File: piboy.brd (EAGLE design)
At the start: 76.2 x 76.2 mm, 69 parts, among them CN4 MicroUSB, T1 MMUN2133LT1G, U1 TPS61090RSAR, U2 MCP73871, U3 TPA2005D1

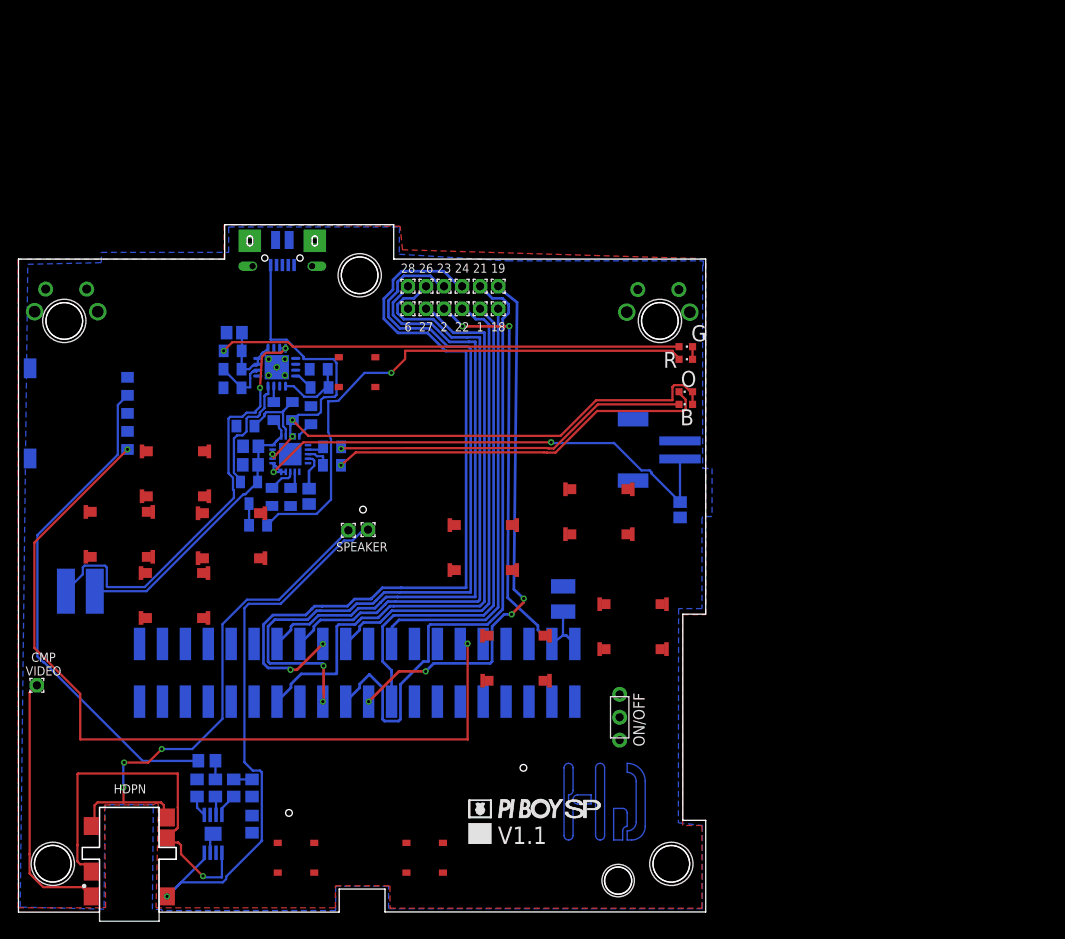
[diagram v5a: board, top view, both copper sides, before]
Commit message: -routed all signals before using the autorouter for voltages and GND
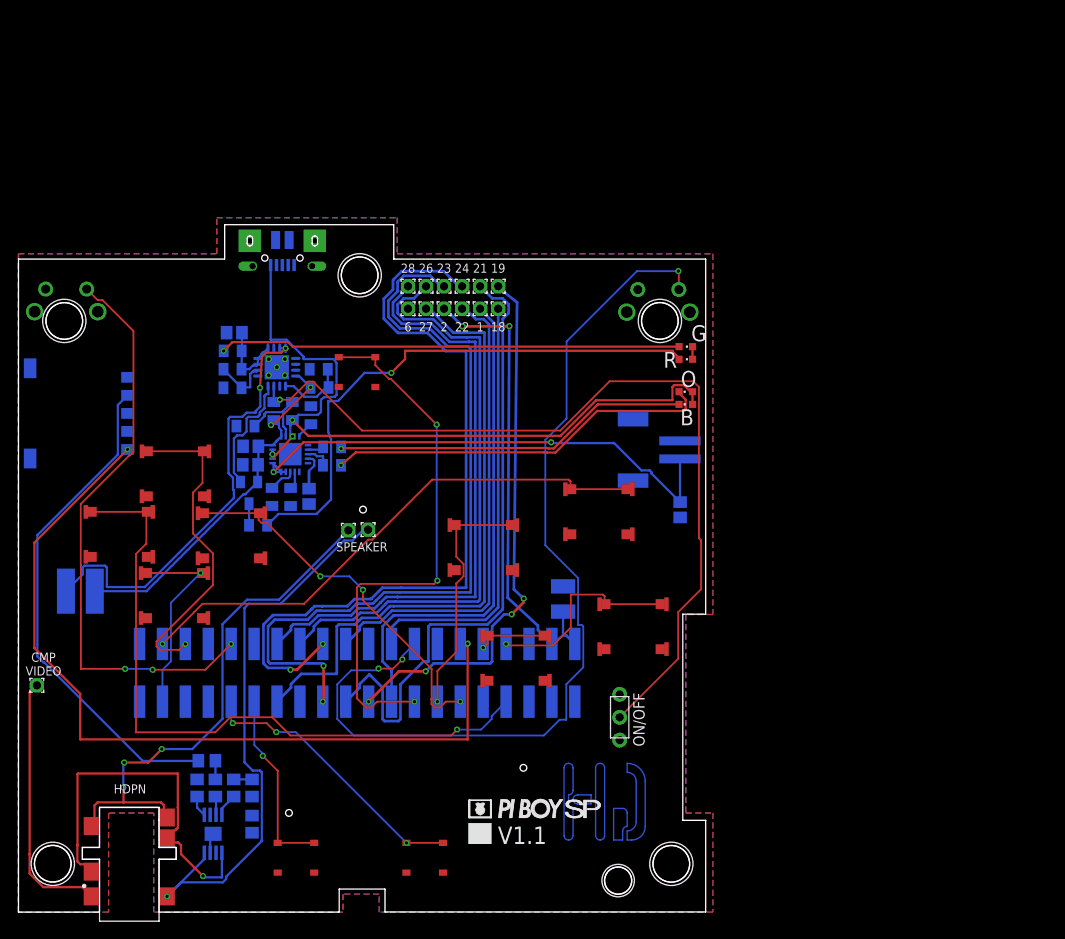
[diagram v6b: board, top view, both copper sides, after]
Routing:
- net J_RSH: track 0.00 -> 104.7 mm, vias 0 -> 3
- net ENABLE: track 1.77 -> 95.1 mm, vias 0 -> 1
- net J_LFT: track 0.00 -> 75.3 mm, vias 0 -> 1
- net J_LSH: track 0.00 -> 64.9 mm, vias 0 -> 3
- net J_BRT: track 0.00 -> 60.4 mm, vias 0 -> 3
- net J_X: track 0.00 -> 59.8 mm, vias 0 -> 1
- net J_RGT: track 0.00 -> 41.0 mm, vias 0 -> 3
- net J_UP: track 0.00 -> 35.2 mm, vias 0 -> 1
- net J_ST: track 0.00 -> 31.3 mm, vias 0 -> 3
- net J_Y: track 0.00 -> 27.1 mm, vias 0 -> 1
- net J_A: track 0.00 -> 22.5 mm, vias 0 -> 1
- net J_DWN: track 0.00 -> 22.0 mm, vias 0 -> 1
- net J_SEL: track 0.00 -> 20.8 mm, vias 0 -> 1
- net J_B: track 0.00 -> 8.05 mm, vias 0 -> 1
- net VBAT: track 34.4 -> 41.2 mm, vias 0 -> 2
- added copper zone on layer 1, net N$18
- removed copper zone on layer 1, net GND

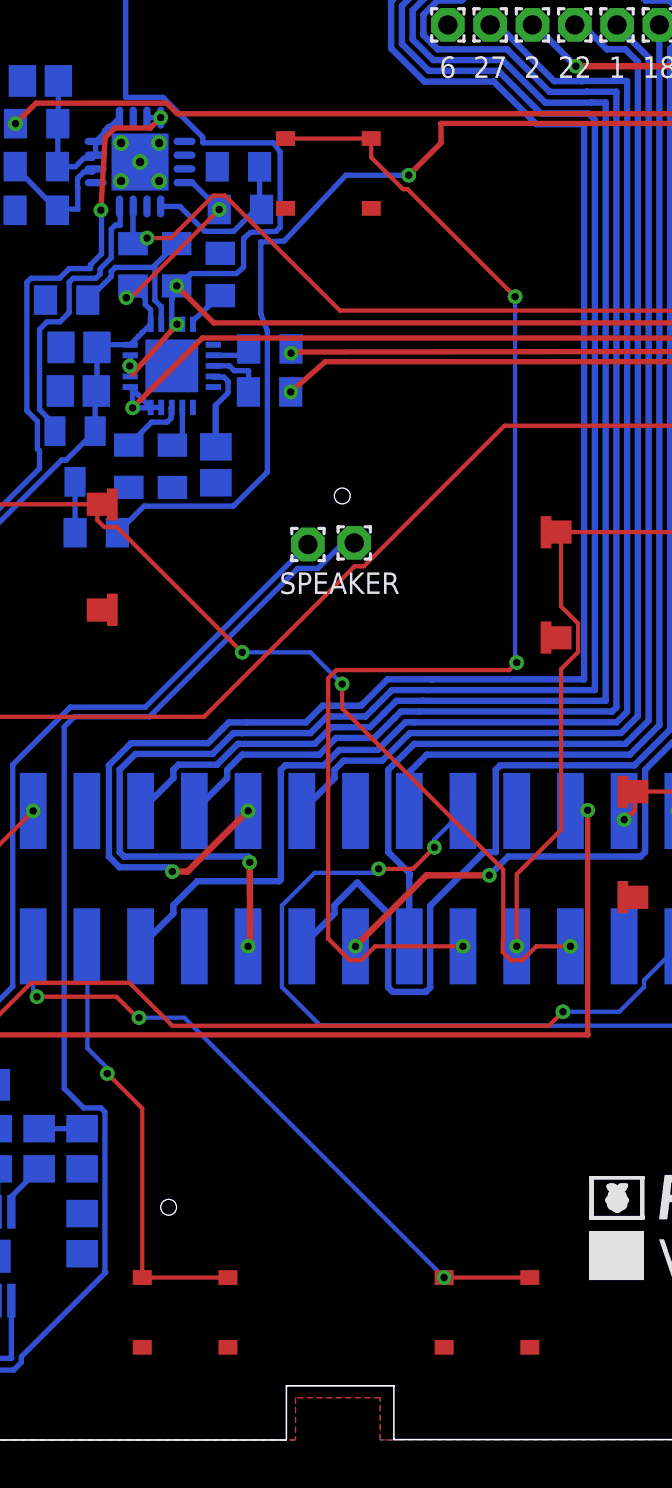
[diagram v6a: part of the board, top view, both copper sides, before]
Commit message: -fixed small button pads
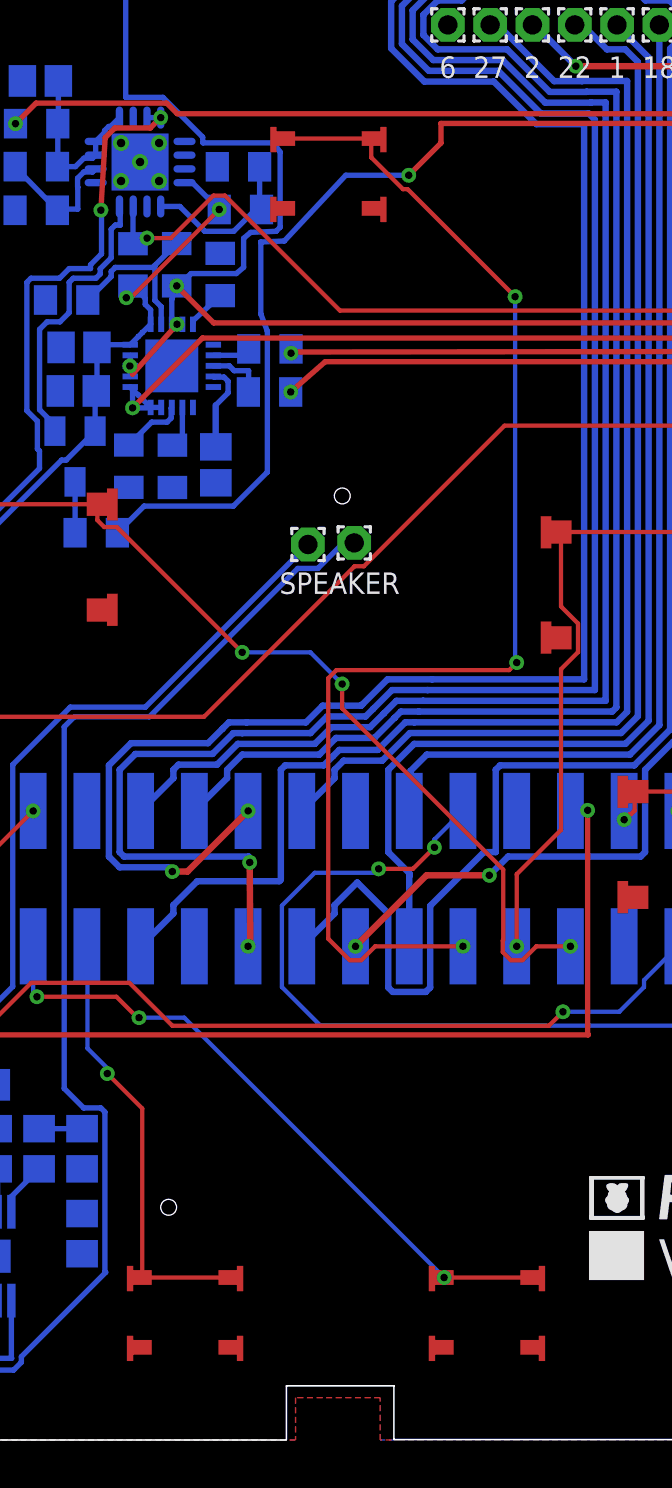
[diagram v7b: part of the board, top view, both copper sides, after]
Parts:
- U$21, U$22, U$25: value TL3315NF100Q -> PIBOY_TL3315NF100Q; device piboy:TL3315NF100Q -> piboy_new:PIBOY_TL3315NF100Q
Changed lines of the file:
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@@
 <element name="U$17" library="piboy_new" package="PIBOY_SKRRAAE010" value="PIBOY_SKRRAAE010" x="68.154" y="31.654"/>
 <element name="U$18" library="piboy_new" package="PIBOY_SKRRAAE010" value="PIBOY_SKRRAAE010" x="55.18" y="28.154"/>
-<element name="U$21" library="piboy" package="TL3315NF100Q" value="TL3315NF100Q" x="30.7776" y="6.03"/>
-<element name="U$22" library="piboy" package="TL3315NF100Q" value="TL3315NF100Q" x="45.05" y="6.03"/>
-<element name="U$25" library="piboy" package="TL3315NF100Q" value="TL3315NF100Q" x="37.5536" y="59.877"/>
+<element name="U$21" library="piboy_new" package="PIBOY_TL3315NF100Q" value="PIBOY_TL3315NF100Q" x="30.7776" y="6.03"/>
+<element name="U$22" library="piboy_new" package="PIBOY_TL3315NF100Q" value="PIBOY_TL3315NF100Q" x="45.05" y="6.03"/>
+<element name="U$25" library="piboy_new" package="PIBOY_TL3315NF100Q" value="PIBOY_TL3315NF100Q" x="37.5536" y="59.877"/>
 <element name="U$26" library="piboy_new" package="SWITCH_TL1105L-4,3" value="SWITCH_TL1105L-4,3" x="5.3006" y="69.0778" rot="R180"/>
 <element name="U$28" library="piboy_new" package="SWITCH_TL1105L-4,3" value="SWITCH_TL1105L-4,3" x="70.9524" y="69.027" rot="R180"/>

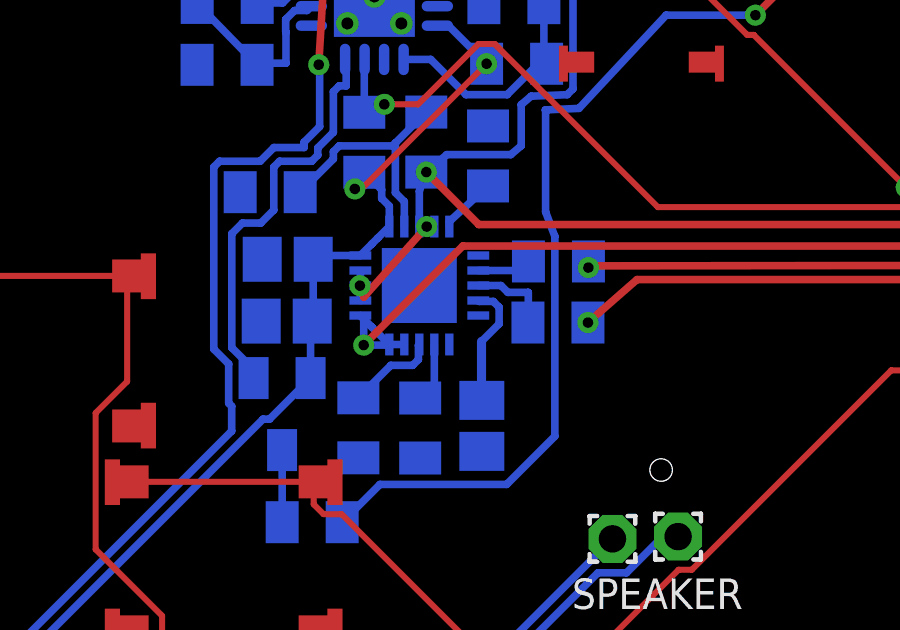
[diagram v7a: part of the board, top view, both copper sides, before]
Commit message: -fixed ground plane issue
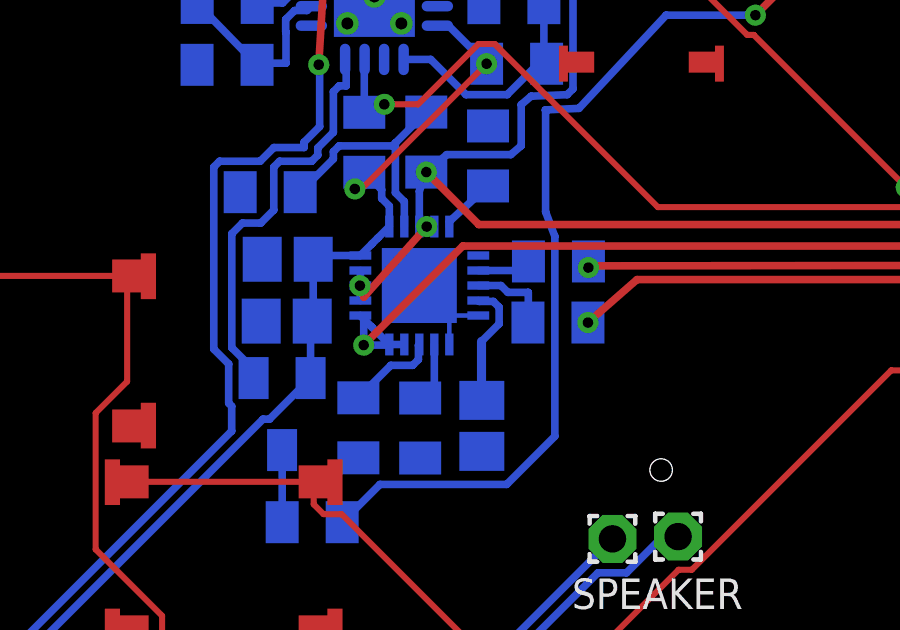
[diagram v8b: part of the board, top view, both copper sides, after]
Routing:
- net GND: track 3.63 -> 8.39 mm
- added copper zone on layer 1, net GND
- removed copper zone on layer 1, net N$18
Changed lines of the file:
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@@
 <grid distance="1" unitdist="mil" unit="mil" style="lines" multiple="1" display="yes" altdistance="0.025" altunitdist="inch" altunit="inch"/>
 <layers>
-<layer number="1" name="Top" color="4" fill="1" visible="yes" active="yes"/>
+<layer number="1" name="Top" color="4" fill="1" visible="no" active="yes"/>
 <layer number="2" name="Route2" color="1" fill="3" visible="no" active="no"/>
 <layer number="3" name="Route3" color="4" fill="3" visible="no" active="no"/>
@@
 <layer number="19" name="Unrouted" color="6" fill="1" visible="yes" active="yes"/>
 <layer number="20" name="Dimension" color="15" fill="1" visible="yes" active="yes"/>
-<layer number="21" name="tPlace" color="63" fill="1" visible="yes" active="yes"/>
+<layer number="21" name="tPlace" color="63" fill="1" visible="no" active="yes"/>
 <layer number="22" name="bPlace" color="63" fill="13" visible="yes" active="yes"/>
-<layer number="23" name="tOrigins" color="15" fill="1" visible="yes" active="yes"/>
+<layer number="23" name="tOrigins" color="15" fill="1" visible="no" active="yes"/>
 <layer number="24" name="bOrigins" color="15" fill="1" visible="yes" active="yes"/>
-<layer number="25" name="tNames" color="7" fill="1" visible="yes" active="yes"/>
+<layer number="25" name="tNames" color="7" fill="1" visible="no" active="yes"/>
 <layer number="26" name="bNames" color="7" fill="1" visible="yes" active="yes"/>
-<layer number="27" name="tValues" color="7" fill="1" visible="yes" active="yes"/>
-<layer number="28" name="bValues" color="7" fill="1" visible="yes" active="yes"/>
+<layer number="27" name="tValues" color="7" fill="1" visible="no" active="yes"/>
+<layer number="28" name="bValues" color="7" fill="1" visible="no" active="yes"/>
 <layer number="29" name="tStop" color="7" fill="3" visible="no" active="yes"/>
 <layer number="30" name="bStop" color="7" fill="6" visible="no" active="yes"/>
@@
 <layer number="37" name="tTest" color="7" fill="1" visible="no" active="yes"/>
 <layer number="38" name="bTest" color="7" fill="1" visible="no" active="yes"/>
-<layer number="39" name="tKeepout" color="4" fill="11" visible="yes" active="yes"/>
+<layer number="39" name="tKeepout" color="4" fill="11" visible="no" active="yes"/>
 <layer number="40" name="bKeepout" color="1" fill="11" visible="yes" active="yes"/>
-<layer number="41" name="tRestrict" color="4" fill="10" visible="yes" active="yes"/>
+<layer number="41" name="tRestrict" color="4" fill="10" visible="no" active="yes"/>
 <layer number="42" name="bRestrict" color="1" fill="10" visible="yes" active="yes"/>
 <layer number="43" name="vRestrict" color="2" fill="10" visible="no" active="yes"/>
-<layer number="44" name="Drills" color="7" fill="1" visible="yes" active="yes"/>
+<layer number="44" name="Drills" color="7" fill="1" visible="no" active="yes"/>
 <layer number="45" name="Holes" color="7" fill="1" visible="yes" active="yes"/>
 <layer number="46" name="Milling" color="3" fill="1" visible="no" active="yes"/>
@@
 <layer number="49" name="Reference" color="7" fill="1" visible="no" active="yes"/>
 <layer number="50" name="dxf" color="7" fill="1" visible="no" active="no"/>
-<layer number="51" name="tDocu" color="7" fill="1" visible="yes" active="yes"/>
+<layer number="51" name="tDocu" color="7" fill="1" visible="no" active="yes"/>
 <layer number="52" name="bDocu" color="7" fill="1" visible="yes" active="yes"/>
 <layer number="53" name="tGND_GNDA" color="7" fill="9" visible="no" active="no"/>
@@
 <wire x1="21.265" y1="6.5868" x2="21.265" y2="8.3618" width="0.254" layer="16"/>
 <wire x1="21.265" y1="8.3618" x2="21.59" y2="8.6868" width="0.254" layer="16"/>
-<wire x1="35.5286" y1="58.227" x2="32.4394" y2="56.0996" width="0" layer="19" extent="1-16"/>
-<wire x1="30.7506" y1="61.3916" x2="29.5506" y2="61.3166" width="0" layer="19" extent="16-16"/>
-<wire x1="26.5506" y1="59.4416" x2="27.7506" y2="59.5166" width="0" layer="19" extent="16-16"/>
-<wire x1="28.9756" y1="58.3166" x2="29.5506" y2="59.5166" width="0" layer="19" extent="16-16"/>
-<wire x1="31.1492" y1="48.8148" x2="32.2326" y2="45.251" width="0" layer="19" extent="16-16"/>
-<wire x1="32.1142" y1="49.7798" x2="31.1492" y2="48.8148" width="0" layer="19" extent="16-16"/>
-<wire x1="30.1492" y1="50.7798" x2="31.1492" y2="48.8148" width="0" layer="19" extent="16-16"/>
-<wire x1="24.178" y1="53.8922" x2="22.7404" y2="58.1358" width="0" layer="19" extent="16-16"/>
-<wire x1="24.9128" y1="51.6548" x2="24.178" y2="53.8922" width="0" layer="19" extent="16-16"/>
-<wire x1="46.455" y1="29.738" x2="52.18" y2="25.654" width="0" layer="19" extent="1-16"/>
 <polygon width="0.2032" layer="16">
 <vertex x="0" y="0"/>
@@
 <vertex x="10" y="0"/>
 </polygon>
+<polygon width="0.2032" layer="1">
+<vertex x="0" y="0"/>
+<vertex x="0" y="73"/>
+<vertex x="22" y="73"/>
+<vertex x="22" y="77"/>
+<vertex x="42" y="77"/>
+<vertex x="42" y="73"/>
+<vertex x="77" y="73"/>
+<vertex x="77" y="33"/>
+<vertex x="74" y="33"/>
+<vertex x="74" y="11"/>
+<vertex x="77" y="11"/>
+<vertex x="77" y="0"/>
+<vertex x="41" y="0"/>
+<vertex x="40" y="0"/>
+<vertex x="40" y="2"/>
+<vertex x="36" y="2"/>
+<vertex x="36" y="0"/>
+<vertex x="15" y="0"/>
+<vertex x="15" y="11"/>
+<vertex x="10" y="11"/>
+<vertex x="10" y="0"/>
+</polygon>
+<wire x1="31.1492" y1="48.8148" x2="31.1492" y2="49.7798" width="0.1524" layer="16"/>
+<wire x1="30.1492" y1="50.7798" x2="31.1492" y2="49.7798" width="0.1524" layer="16"/>
+<wire x1="32.1142" y1="49.7798" x2="31.1492" y2="49.7798" width="0.1524" layer="16"/>
+<wire x1="31.1492" y1="49.7798" x2="30.1492" y2="50.7798" width="0.1524" layer="16"/>
+<wire x1="35.5286" y1="58.227" x2="32.4394" y2="56.0996" width="0" layer="19" extent="1-16"/>
+<wire x1="30.7506" y1="61.3916" x2="29.5506" y2="61.3166" width="0" layer="19" extent="16-16"/>
+<wire x1="28.9756" y1="58.3166" x2="29.5506" y2="59.5166" width="0" layer="19" extent="16-16"/>
+<wire x1="32.2326" y1="45.251" x2="30.178" y2="45.0302" width="0" layer="19" extent="16-16"/>
+<wire x1="51.535" y1="23.338" x2="52.18" y2="25.654" width="0" layer="19" extent="1-16"/>
+<wire x1="31.1492" y1="48.8148" x2="32.2326" y2="45.251" width="0" layer="19" extent="16-16"/>
+<wire x1="24.178" y1="53.8922" x2="22.7404" y2="58.1358" width="0" layer="19" extent="16-16"/>
+<wire x1="24.9128" y1="51.6548" x2="24.178" y2="53.8922" width="0" layer="19" extent="16-16"/>
+<wire x1="26.6282" y1="39.2362" x2="28.1166" y2="45.037" width="0" layer="19" extent="1-16"/>
+<wire x1="14.4104" y1="46.1" x2="20.4104" y2="46.1" width="0" layer="19" extent="1-1"/>
+<wire x1="8.187" y1="39.387" x2="14.187" y2="39.387" width="0" layer="19" extent="1-1"/>
+<wire x1="46.455" y1="29.738" x2="52.18" y2="25.654" width="0" layer="19" extent="1-16"/>
+<wire x1="74.75" y1="62.7" x2="68.6774" y2="69.027" width="0" layer="19" extent="1-1"/>
 </signal>
 <signal name="N$1">
@@
 <wire x1="32.615975" y1="50.25" x2="32.8094" y2="50.056575" width="0.254" layer="16"/>
 <wire x1="32.8094" y1="50.056575" x2="32.8094" y2="49.503025" width="0.254" layer="16"/>
-<wire x1="32.1142" y1="50.2798" x2="32.144" y2="50.25" width="0.254" layer="16"/>
+<wire x1="32.144" y1="50.25" x2="32.1142" y2="50.2798" width="0.254" layer="16"/>
 <wire x1="32.144" y1="50.25" x2="32.615975" y2="50.25" width="0.254" layer="16"/>
 <wire x1="32.8094" y1="49.503025" x2="32.223" y2="48.916625" width="0.254" layer="16"/>
@@
 <wire x1="28.8986" y1="34.6456" x2="36.587" y2="42.334" width="0.254" layer="16"/>
 </signal>
-<signal name="N$18">
-<polygon width="0.2032" layer="1">
-<vertex x="0" y="0"/>
-<vertex x="0" y="73"/>
-<vertex x="22" y="73"/>
-<vertex x="22" y="77"/>
-<vertex x="42" y="77"/>
-<vertex x="42" y="73"/>
-<vertex x="77" y="73"/>
-<vertex x="77" y="33"/>
-<vertex x="74" y="33"/>
-<vertex x="74" y="11"/>
-<vertex x="77" y="11"/>
-<vertex x="77" y="0"/>
-<vertex x="41" y="0"/>
-<vertex x="40" y="0"/>
-<vertex x="40" y="2"/>
-<vertex x="36" y="2"/>
-<vertex x="36" y="0"/>
-<vertex x="15" y="0"/>
-<vertex x="15" y="11"/>
-<vertex x="10" y="11"/>
-<vertex x="10" y="0"/>
-</polygon>
-</signal>
 </signals>
